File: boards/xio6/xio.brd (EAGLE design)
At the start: 170 x 100 mm, 35 parts, among them IC1 STM32MP157AAA3, IC2 IS43TR16256AL-125KBL, IC3 TFP410PAP, IC4 STPMIC1APQR, J1 DC-005, J3 RJMG2310228A0ER

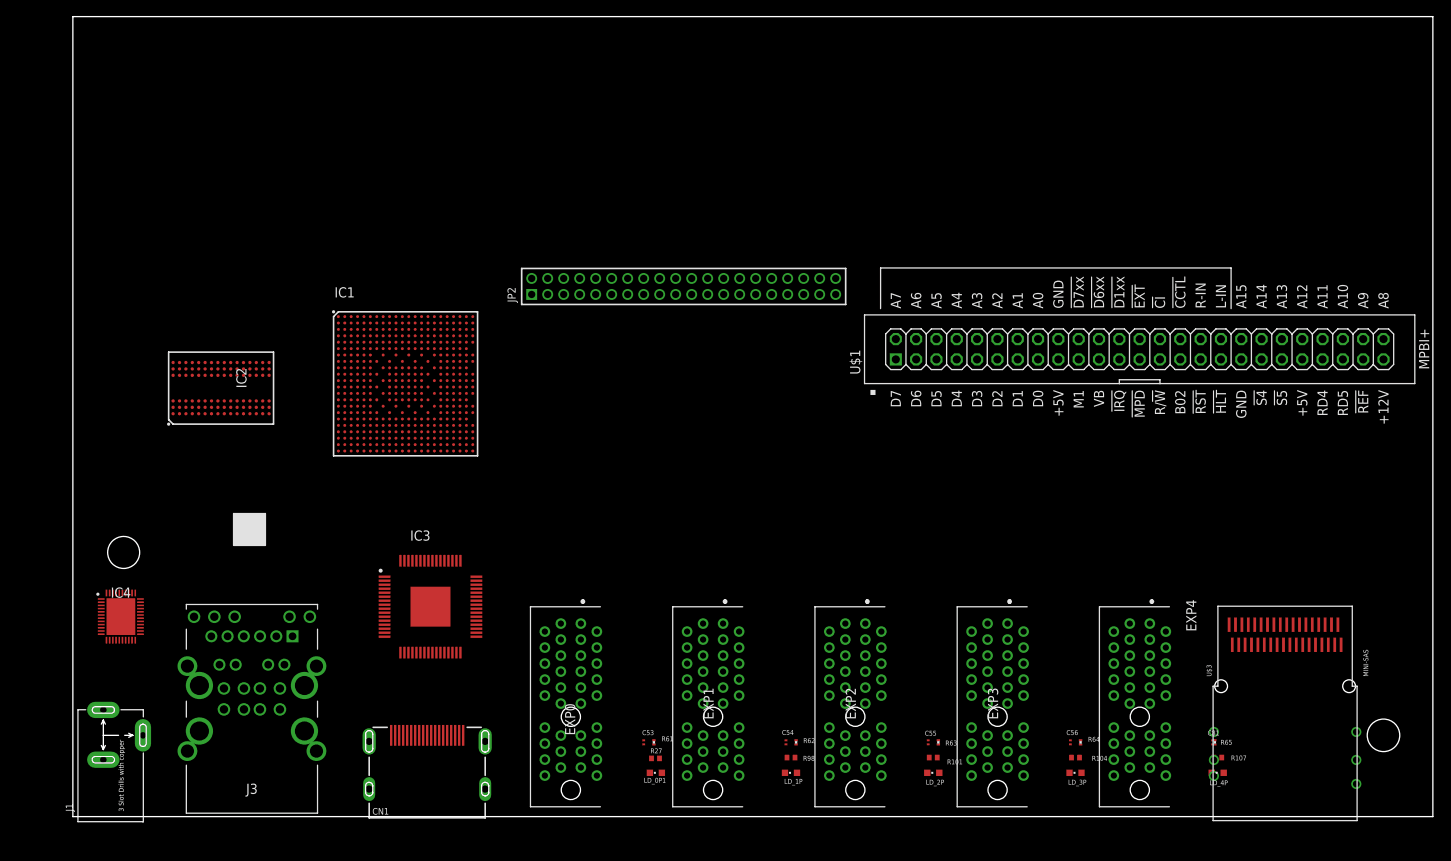
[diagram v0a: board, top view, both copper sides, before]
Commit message: Get the smaller PCIe slots organised
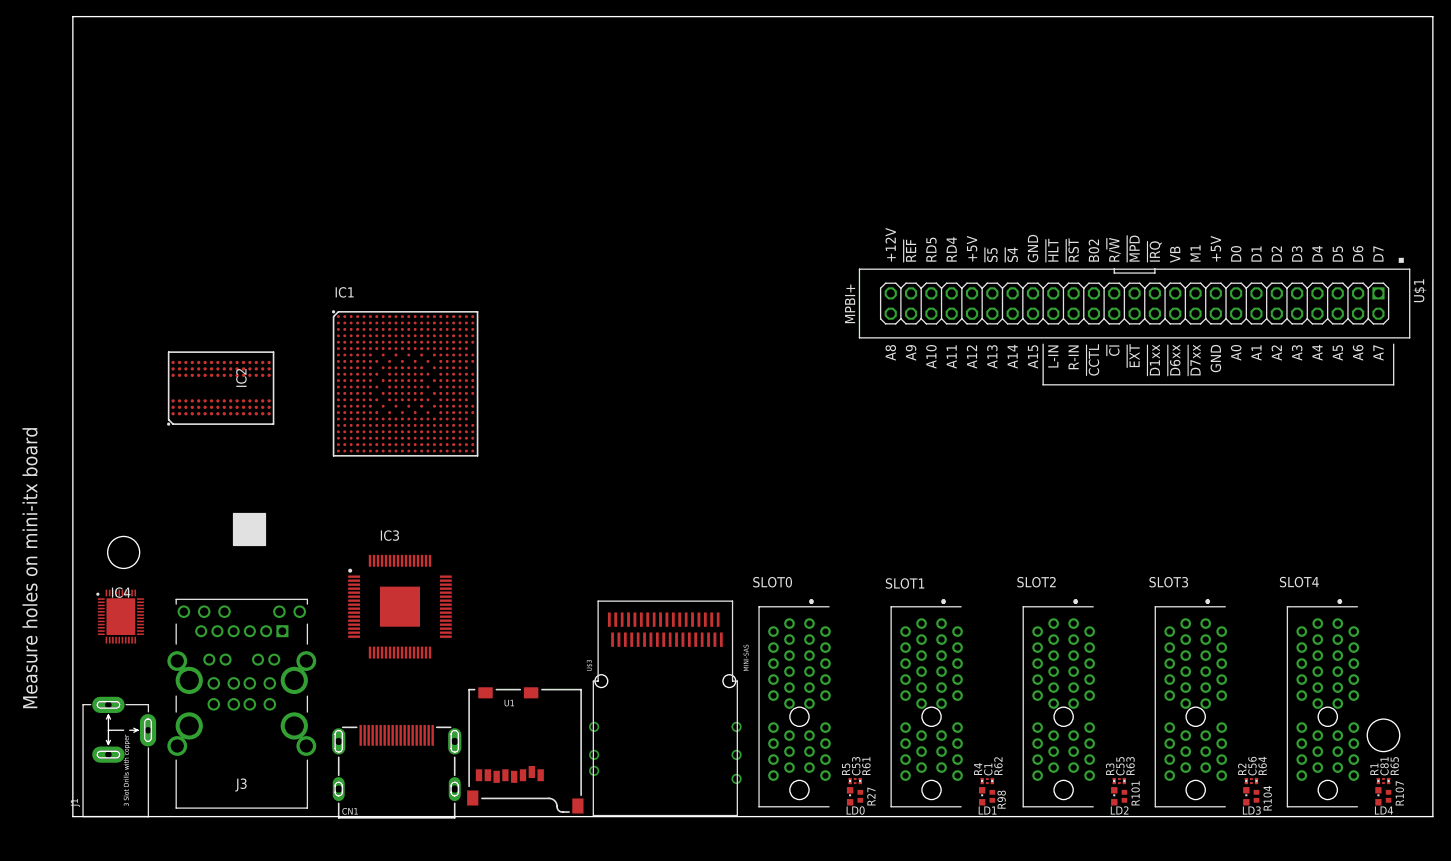
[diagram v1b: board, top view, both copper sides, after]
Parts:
- removed C54: 0.1uF, rcl:C0201
- removed EXP0, EXP1, EXP2, EXP3, EXP4: 10018784-10210TLF, samacsys:1001878410210TLF
- removed JP2: (no value), pinhead-2:2X20M
- removed LD_0P1, LD_1P, LD_2P, LD_3P, LD_4P: SML-D12D1WT86, led:CHIPLED_0603
- added C1: 0.1uF, rcl:C0201
- added LD0, LD1, LD2, LD3, LD4: SML-D12D1WT86, led:CHIPLED_0603
- added R1, R2, R3, R4, R5: 10K, rcl:R0201
- added SLOT0, SLOT1, SLOT2, SLOT3, SLOT4: 10018784-10210TLF, samacsys:1001878410210TLF
- added U1: USD-SOCKETNEW, SparkFun:MICRO-SD-SOCKET-PP
- moved U$3 77.5 mm to (73.7, 13.3)
- moved C53 26.9 mm to (97.8, 4.45)
- moved R61 26.3 mm to (98.4, 4.45), turned to 90 degrees
- moved R27 26.0 mm to (98.4, 2.54), turned to 270 degrees
- moved R98 25.6 mm to (114.9, 2.54), turned to 270 degrees
- moved R62 25.0 mm to (114.9, 4.45)
- moved C55 24.4 mm to (130.8, 4.45)
- moved R101 24.4 mm to (131.4, 2.54), turned to 270 degrees
- moved R63 23.8 mm to (131.4, 4.45), turned to 90 degrees
- moved R104 23.1 mm to (148.0, 2.54), turned to 270 degrees
- moved C56 23.1 mm to (147.3, 4.45)
- moved R64 22.5 mm to (148.0, 4.45), turned to 90 degrees
- moved R65 22.3 mm to (164.5, 4.45)
- moved C81 21.9 mm to (163.8, 4.45)
- moved R107 21.9 mm to (164.5, 2.54), turned to 270 degrees
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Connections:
- net !HI_CCTL! renamed !CCTL!
- net !HI_EXTSEL! renamed !EXTSEL!
- net !HI_HALT! renamed !HALT!
- net !HI_IRQ! renamed !IRQ!
- net !HI_MPD! renamed !MPD!
- net !HI_RST! renamed !RST!
- net !HI_S4! renamed !S4!
- net !HI_S5! renamed !S5!
- net HI_CLK renamed CLK
- net HI_R/!W! renamed R/!W!
- net HI_RD4 renamed RD4
- net HI_RD5 renamed RD5
- removed net !LO_EXTSEL!: EXP0.B11, EXP1.B11, EXP2.B11, EXP3.B11, EXP4.B11
- removed net !LO_MPD!: EXP0.B13, EXP1.B13, EXP2.B13, EXP3.B13, EXP4.B13
- removed net !LO_RST!: EXP0.B7, EXP1.B7, EXP2.B7, EXP3.B7, EXP4.B7
- removed net HI_A0: U$1.16, U$3.PA1
- removed net HI_A1: U$1.14, U$3.PB1
- removed net HI_A10: U$1.46, U$3.PA6
- removed net HI_A11: U$1.44, U$3.PB6
- removed net HI_A12: U$1.42, U$3.PA7
- removed net HI_A13: U$1.40, U$3.PB7
- removed net HI_A14: U$1.38, U$3.PA8
- removed net HI_A15: U$1.36, U$3.PB8
- removed net HI_A2: U$1.12, U$3.PA2
- removed net HI_A3: U$1.10, U$3.PB2
- removed net HI_A4: U$1.8, U$3.PA3
- removed net HI_A5: U$1.6, U$3.PB3
- removed net HI_A6: U$1.4, U$3.PA4
- removed net HI_A7: U$1.2, U$3.PB4
- removed net HI_A8: U$1.50, U$3.PA5
- removed net HI_A9: U$1.48, U$3.PB5
- removed net HI_D0: U$1.15, U$3.PB9
- removed net HI_D1: U$1.13, U$3.PA10
- removed net HI_D2: U$1.11, U$3.PB10
- removed net HI_D3: U$1.9, U$3.PA11
- removed net HI_D4: U$1.7, U$3.PB11
- removed net HI_D5: U$1.5, U$3.PA12
- removed net HI_D6: U$1.3, U$3.PB12
- removed net HI_D7: U$1.1, U$3.PA13
- removed net I2C0_SCL: JP2.37
- removed net I2C0_SDA: JP2.35
- removed net LO_A10: EXP0.A13, EXP1.A13, EXP2.A13, EXP3.A13, EXP4.A13
- removed net LO_A11: EXP0.A15, EXP1.A15, EXP2.A15, EXP3.A15, EXP4.A15
- removed net LO_A12: EXP0.A17, EXP1.A17, EXP2.A17, EXP3.A17, EXP4.A17
- removed net LO_A13: EXP0.B1, EXP1.B1, EXP2.B1, EXP3.B1, EXP4.B1
- removed net LO_A14: EXP0.B3, EXP1.B3, EXP2.B3, EXP3.B3, EXP4.B3
- removed net LO_A15: EXP0.B5, EXP1.B5, EXP2.B5, EXP3.B5, EXP4.B5
- removed net LO_A4: EXP0.A1, EXP1.A1, EXP2.A1, EXP3.A1, EXP4.A1
- removed net LO_A5: EXP0.A3, EXP1.A3, EXP2.A3, EXP3.A3, EXP4.A3
- removed net LO_A6: EXP0.A5, EXP1.A5, EXP2.A5, EXP3.A5, EXP4.A5
- removed net LO_A7: EXP0.A7, EXP1.A7, EXP2.A7, EXP3.A7, EXP4.A7
- removed net LO_A8: EXP0.A9, EXP1.A9, EXP2.A9, EXP3.A9, EXP4.A9
- removed net LO_A9: EXP0.A11, EXP1.A11, EXP2.A11, EXP3.A11, EXP4.A11
- removed net LO_CLK: EXP0.B9, EXP1.B9, EXP2.B9, EXP3.B9, EXP4.B9
- removed net LO_R/!W!: EXP0.A2, EXP1.A2, EXP2.A2, EXP3.A2, EXP4.A2
- removed net LO_RD4: EXP0.B15, EXP1.B15, EXP2.B15, EXP3.B15, EXP4.B15
- removed net LO_RD5: EXP0.B17, EXP1.B17, EXP2.B17, EXP3.B17, EXP4.B17
- removed net N$101: LD_4P.A, R107.2
- removed net N$91: LD_1P.A, R98.2
- removed net N$94: LD_2P.A, R101.2
- removed net N$97: LD_3P.A, R104.2
- removed net S0_PRESENT: R27.1, R61.2
- removed net S1_PRESENT: R62.2, R98.1
- removed net S2_PRESENT: R101.1, R63.2
- removed net S3_PRESENT: R104.1, R64.2
- removed net S4_PRESENT: R107.1, R65.2
- removed net S5_PRESENT: JP2.20
- removed net SPI2_CS1: JP2.12
- removed net SPI2_IRQ: JP2.16
- removed net SPI_IRQ5: JP2.22
- removed net XBUS0: JP2.26
- removed net XBUS1: JP2.28
- removed net XBUS2: JP2.30
- removed net XBUS3: JP2.32
- removed net XBUS4: JP2.34
- removed net XBUS5: JP2.36
- removed net XBUS6: JP2.38
- removed net XBUS7: JP2.40
- removed net ZBUS0: EXP0.A4, EXP1.A4, EXP2.A4, EXP3.A4, EXP4.A4, JP2.31
- removed net ZBUS1: EXP0.A6, EXP1.A6, EXP2.A6, EXP3.A6, EXP4.A6, JP2.29
- removed net ZBUS10: EXP0.B6, EXP1.B6, EXP2.B6, EXP3.B6, EXP4.B6, JP2.11
- removed net ZBUS11: EXP0.B8, EXP1.B8, EXP2.B8, EXP3.B8, EXP4.B8, JP2.9
- removed net ZBUS12: EXP0.B10, EXP1.B10, EXP2.B10, EXP3.B10, EXP4.B10, JP2.7
- removed net ZBUS13: EXP0.B12, EXP1.B12, EXP2.B12, EXP3.B12, EXP4.B12, JP2.5
- removed net ZBUS14: EXP0.B14, EXP1.B14, EXP2.B14, EXP3.B14, EXP4.B14, JP2.3
- removed net ZBUS15: EXP0.B16, EXP1.B16, EXP2.B16, EXP3.B16, EXP4.B16, JP2.1
- removed net ZBUS2: EXP0.A8, EXP1.A8, EXP2.A8, EXP3.A8, EXP4.A8, JP2.27
- removed net ZBUS3: EXP0.A10, EXP1.A10, EXP2.A10, EXP3.A10, EXP4.A10, JP2.25
- removed net ZBUS4: EXP0.A12, EXP1.A12, EXP2.A12, EXP3.A12, EXP4.A12, JP2.23
- removed net ZBUS5: EXP0.A14, EXP1.A14, EXP2.A14, EXP3.A14, EXP4.A14, JP2.21
- removed net ZBUS6: EXP0.A16, EXP1.A16, EXP2.A16, EXP3.A16, EXP4.A16, JP2.19
- removed net ZBUS7: EXP0.A18, EXP1.A18, EXP2.A18, EXP3.A18, EXP4.A18, JP2.17
- removed net ZBUS8: EXP0.B2, EXP1.B2, EXP2.B2, EXP3.B2, EXP4.B2, JP2.15
- removed net ZBUS9: EXP0.B4, EXP1.B4, EXP2.B4, EXP3.B4, EXP4.B4, JP2.13
- new net !SP1_IRQ!: R4.2, SLOT1.B10
- new net !SPI0_IRQ!: R5.2, SLOT0.B10
- new net !SPI2_IRQ!: R3.2, SLOT2.B10
- new net !SPI3_IRQ!: R2.2, SLOT3.B10
- new net !SPI4_IRQ!: R1.2, SLOT4.B10
- new net A0: SLOT0.A1, SLOT1.A1, SLOT2.A1, SLOT3.A1, SLOT4.A1, U$1.16, U$3.PA1
- new net A1: SLOT0.A3, SLOT1.A3, SLOT2.A3, SLOT3.A3, SLOT4.A3, U$1.14, U$3.PB1
- new net A10: SLOT0.B3, SLOT1.B3, SLOT2.B3, SLOT3.B3, SLOT4.B3, U$1.46, U$3.PA6
- new net A11: SLOT0.B5, SLOT1.B5, SLOT2.B5, SLOT3.B5, SLOT4.B5, U$1.44, U$3.PB6
- new net A12: SLOT0.B7, SLOT1.B7, SLOT2.B7, SLOT3.B7, SLOT4.B7, U$1.42, U$3.PA7
- new net A13: SLOT0.B9, SLOT1.B9, SLOT2.B9, SLOT3.B9, SLOT4.B9, U$1.40, U$3.PB7
- new net A14: SLOT0.B11, SLOT1.B11, SLOT2.B11, SLOT3.B11, SLOT4.B11, U$1.38, U$3.PA8
- new net A15: SLOT0.B13, SLOT1.B13, SLOT2.B13, SLOT3.B13, SLOT4.B13, U$1.36, U$3.PB8
- new net A2: SLOT0.A5, SLOT1.A5, SLOT2.A5, SLOT3.A5, SLOT4.A5, U$1.12, U$3.PA2
- new net A3: SLOT0.A7, SLOT1.A7, SLOT2.A7, SLOT3.A7, SLOT4.A7, U$1.10, U$3.PB2
- new net A4: SLOT0.A9, SLOT1.A9, SLOT2.A9, SLOT3.A9, SLOT4.A9, U$1.8, U$3.PA3
- new net A5: SLOT0.A11, SLOT1.A11, SLOT2.A11, SLOT3.A11, SLOT4.A11, U$1.6, U$3.PB3
- new net A6: SLOT0.A13, SLOT1.A13, SLOT2.A13, SLOT3.A13, SLOT4.A13, U$1.4, U$3.PA4
- new net A7: SLOT0.A15, SLOT1.A15, SLOT2.A15, SLOT3.A15, SLOT4.A15, U$1.2, U$3.PB4
- new net A8: SLOT0.A17, SLOT1.A17, SLOT2.A17, SLOT3.A17, SLOT4.A17, U$1.50, U$3.PA5
- new net A9: SLOT0.B1, SLOT1.B1, SLOT2.B1, SLOT3.B1, SLOT4.B1, U$1.48, U$3.PB5
- new net AVALID: SLOT0.B15, SLOT1.B15, SLOT2.B15, SLOT3.B15, SLOT4.B15
- new net D0: SLOT0.A10, SLOT1.A10, SLOT2.A10, SLOT3.A10, SLOT4.A10, U$1.15, U$3.PB9
- new net D1: SLOT0.A12, SLOT1.A12, SLOT2.A12, SLOT3.A12, SLOT4.A12, U$1.13, U$3.PA10
- new net D2: SLOT0.A14, SLOT1.A14, SLOT2.A14, SLOT3.A14, SLOT4.A14, U$1.11, U$3.PB10
- new net D3: SLOT0.A16, SLOT1.A16, SLOT2.A16, SLOT3.A16, SLOT4.A16, U$1.9, U$3.PA11
- new net D4: SLOT0.A18, SLOT1.A18, SLOT2.A18, SLOT3.A18, SLOT4.A18, U$1.7, U$3.PB11
- new net D5: SLOT0.B2, SLOT1.B2, SLOT2.B2, SLOT3.B2, SLOT4.B2, U$1.5, U$3.PA12
- new net D6: SLOT0.B4, SLOT1.B4, SLOT2.B4, SLOT3.B4, SLOT4.B4, U$1.3, U$3.PB12
- new net D7: SLOT0.B6, SLOT1.B6, SLOT2.B6, SLOT3.B6, SLOT4.B6, U$1.1, U$3.PA13
- new net N$10: LD4.A, R107.2
- new net N$3: LD1.A, R98.2
- new net N$5: LD0.A, R27.2
- new net N$6: R104.1, R64.1, SLOT3.A8
- new net N$7: R101.1, R63.1, SLOT2.A8
- new net N$8: LD3.A, R104.2
- new net N$9: R107.1, R65.1, SLOT4.A8
- new net PRESENT0: R62.1, R98.1, SLOT0.A8
- new net PRESENT1: R27.1, R61.1, SLOT1.A8
- new net SPI0_CLK: SLOT0.B12
- new net SPI0_MISO: SLOT0.B14
- new net SPI0_MOSI: SLOT0.B16
- new net SPI1_CLK: SLOT1.B12
- new net SPI1_MISO: SLOT1.B14
- new net SPI1_MOSI: SLOT1.B16
- new net SPI3_CLK: SLOT3.B12
- new net SPI3_MISO: SLOT3.B14
- new net SPI3_MOSI: SLOT3.B16
- new net SPI4_CLK: SLOT4.B12
- new net SPI4_MISO: SLOT4.B14
- new net SPI4_MOSI: SLOT4.B16
- net +3V3: now also SLOT0.A2, SLOT1.A2, SLOT2.A2, SLOT3.A2, SLOT4.A2; no longer JP2.6, JP2.8
- net +5V: now also C1.1, C56.2, R1.1, R2.1, R3.1, R4.1, R5.1, SLOT0.A4, SLOT0.A6, SLOT1.A4, SLOT1.A6, SLOT2.A4, SLOT2.A6, SLOT3.A4, SLOT3.A6, SLOT4.A4, SLOT4.A6; no longer C54.1, C56.1, JP2.2, JP2.4
- net GND: now also C1.2, C56.1, LD0.C, LD1.C, LD2.C, LD3.C, LD4.C, R61.2, R62.2, R63.2, R64.2, R65.2, SLOT0.B17, SLOT0.B18, SLOT0.B8, SLOT1.B17, SLOT1.B18, SLOT1.B8, SLOT2.B17, SLOT2.B18, SLOT2.B8, SLOT3.B17, SLOT3.B18, SLOT3.B8, SLOT4.B17, SLOT4.B18, SLOT4.B8; no longer C54.2, C56.2, EXP0.B18, EXP1.B18, EXP2.B18, EXP3.B18, EXP4.B18, JP2.24, JP2.33, JP2.39, LD_0P1.C, LD_1P.C, LD_2P.C, LD_3P.C, LD_4P.C, R61.1, R62.1, R63.1, R64.1, R65.1
- net N$1: now also LD2.A, R101.2; no longer LD_0P1.A, R27.2
- net SPI2_CLK: now also SLOT2.B12; no longer JP2.10
- net SPI2_MISO: now also SLOT2.B14; no longer JP2.14
- net SPI2_MOSI: now also SLOT2.B16; no longer JP2.18
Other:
- board text added: "Measure holes on mini-itx board"

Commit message: More work on the dual-core STM
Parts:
- removed U1: USD-SOCKETNEW, SparkFun:MICRO-SD-SOCKET-PP
- added J2: MICROSD_MOLEX_5025700893, j_microsd_molex_5025700893:5025700893
- moved U$3 3.64 mm to (73.7, 9.70)
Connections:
- new net SH1: J2.GND0
- new net SH2: J2.GND1
- new net SH3: J2.GND2
- new net SH4: J2.GND3
- new net SH5: J2.GND4
- new net VDD: J2.P$4
- new net VSS: J2.P$6
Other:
- board text added: "Should be 3.7mm past edge"
